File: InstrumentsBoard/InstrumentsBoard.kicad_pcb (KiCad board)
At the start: 2 copper layers, 105.7 x 47.1 mm, 27 parts, among them J1 RJ45_LED_Shielded, Q1 BSS138, Q2 BSS138, Q3 BSS138BK, U1 Teensy4.1_DEV-16771, U2 OKI

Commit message: board review changes
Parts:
- removed R8, R9: 4.7k, Resistor_SMD:R_0603_1608Metric_Pad0.98x0.95mm_HandSolder
- moved C2 12.9 mm to (107.4, 66.0), turned to -90 degrees
- moved C3 5.83 mm to (94.0, 66.2), turned to -90 degrees
- moved Conn5 2.29 mm to (65.0, 67.3)
- moved Q3 1.68 mm to (65.0, 59.8)
- moved U2 1.02 mm to (98.0, 58.0)
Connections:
- Conn5 pad 1: GND -> Net-(Q3-D)
- Conn5 pad 2: Green_Laser_5V -> +5V
- Q3 pad 1: +3V3 -> Green_Laser_3V3
- Q3 pad 2: Green_Laser_3V3 -> GND
- Q3 pad 3: Green_Laser_5V -> Net-(Q3-D)
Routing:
- net Green_Laser_5V: track 15.5 -> 0.00 mm
- net +3V3: track 152.8 -> 139.7 mm, vias 4 -> 3
- net Green_Laser_3V3: track 19.3 -> 7.37 mm
- net Net-(Q3-D): track 0.00 -> 6.96 mm
- net +5V: track 146.3 -> 147.8 mm
- net +12V: track 87.3 -> 86.2 mm
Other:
- board text removed: "5V Signal"

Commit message: fix low side toggle circuit
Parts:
- added R8: 4.7k, Resistor_SMD:R_0603_1608Metric_Pad0.98x0.95mm_HandSolder, F.Cu at (65.0, 56.4)
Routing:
- net Green_Laser_3V3: track 7.37 -> 9.83 mm
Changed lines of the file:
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@@
+  )
+  (footprint "Resistor_SMD:R_0603_1608Metric_Pad0.98x0.95mm_HandSolder" (layer "F.Cu")
+    (at 65.024 56.388 180)
+    (descr "Resistor SMD 0603 (1608 Metric), square (rectangular) end terminal, IPC_7351 nominal with elongated pad for handsoldering. (Body size source: IPC-SM-782 page 72, https://www.pcb-3d.com/wordpress/wp-content/uploads/ipc-sm-782a_amendment_1_and_2.pdf), generated with kicad-footprint-generator")
+    (tags "resistor handsolder")
+    (property "Sheetfile" "InstrumentsBoard.kicad_sch")
+    (property "Sheetname" "")
+    (property "ki_description" "Resistor")
+    (property "ki_keywords" "R res resistor")
+    (attr smd)
+    (fp_text reference "R8" (at 0 -1.43) (layer "F.SilkS")
+        (effects (font (size 1 1) (thickness 0.15)))
+    )
+    (fp_text value "4.7k" (at 0 1.43) (layer "F.Fab")
+        (effects (font (size 1 1) (thickness 0.15)))
+    )
+    (fp_text user "${REFERENCE}" (at 0 0) (layer "F.Fab")
+        (effects (font (size 0.4 0.4) (thickness 0.06)))
+    )
+    (fp_line (start -0.254724 -0.5225) (end 0.254724 -0.5225)
+      (stroke (width 0.12) (type solid)) (layer "F.SilkS"))
+    (fp_line (start -0.254724 0.5225) (end 0.254724 0.5225)
+      (stroke (width 0.12) (type solid)) (layer "F.SilkS"))
+    (fp_line (start -1.65 -0.73) (end 1.65 -0.73)
+      (stroke (width 0.05) (type solid)) (layer "F.CrtYd"))
+    (fp_line (start -1.65 0.73) (end -1.65 -0.73)
+      (stroke (width 0.05) (type solid)) (layer "F.CrtYd"))
+    (fp_line (start 1.65 -0.73) (end 1.65 0.73)
+      (stroke (width 0.05) (type solid)) (layer "F.CrtYd"))
+    (fp_line (start 1.65 0.73) (end -1.65 0.73)
+      (stroke (width 0.05) (type solid)) (layer "F.CrtYd"))
+    (fp_line (start -0.8 -0.4125) (end 0.8 -0.4125)
+      (stroke (width 0.1) (type solid)) (layer "F.Fab"))
+    (fp_line (start -0.8 0.4125) (end -0.8 -0.4125)
+      (stroke (width 0.1) (type solid)) (layer "F.Fab"))
+    (fp_line (start 0.8 -0.4125) (end 0.8 0.4125)
+      (stroke (width 0.1) (type solid)) (layer "F.Fab"))
+    (fp_line (start 0.8 0.4125) (end -0.8 0.4125)
+      (stroke (width 0.1) (type solid)) (layer "F.Fab"))
+    (pad "1" smd roundrect (at -0.9125 0 180) (size 0.975 0.95) (layers "F.Cu" "F.Paste" "F.Mask") (roundrect_rratio 0.25)
+      (net 9 "Green_Laser_3V3") (pintype "passive"))
+    (pad "2" smd roundrect (at 0.9125 0 180) (size 0.975 0.95) (layers "F.Cu" "F.Paste" "F.Mask") (roundrect_rratio 0.25)
+      (net 2 "GND") (pintype "passive"))
+    (model "${KICAD6_3DMODEL_DIR}/Resistor_SMD.3dshapes/R_0603_1608Metric.wrl"
+      (offset (xyz 0 0 0))
+      (scale (xyz 1 1 1))
+      (rotate (xyz 0 0 0))
+    )
   )
   (footprint "Resistor_SMD:R_0603_1608Metric_Pad0.98x0.95mm_HandSolder" (layer "F.Cu")
@@
   (segment (start 65.974 58.74) (end 65.974 58.831) (width 0.25) (layer "F.Cu") (net 9))
   (segment (start 71.12 53.594) (end 65.974 58.74) (width 0.25) (layer "F.Cu") (net 9))
+  (segment (start 65.9365 58.7935) (end 65.974 58.831) (width 0.25) (layer "F.Cu") (net 9))
+  (segment (start 65.9365 56.388) (end 65.9365 58.7935) (width 0.25) (layer "F.Cu") (net 9))
   (segment (start 38.899 48.223) (end 44.318 42.804) (width 0.254) (layer "F.Cu") (net 11))
   (segment (start 31.9645 47.523) (end 32.6645 48.223) (width 0.254) (layer "F.Cu") (net 11))

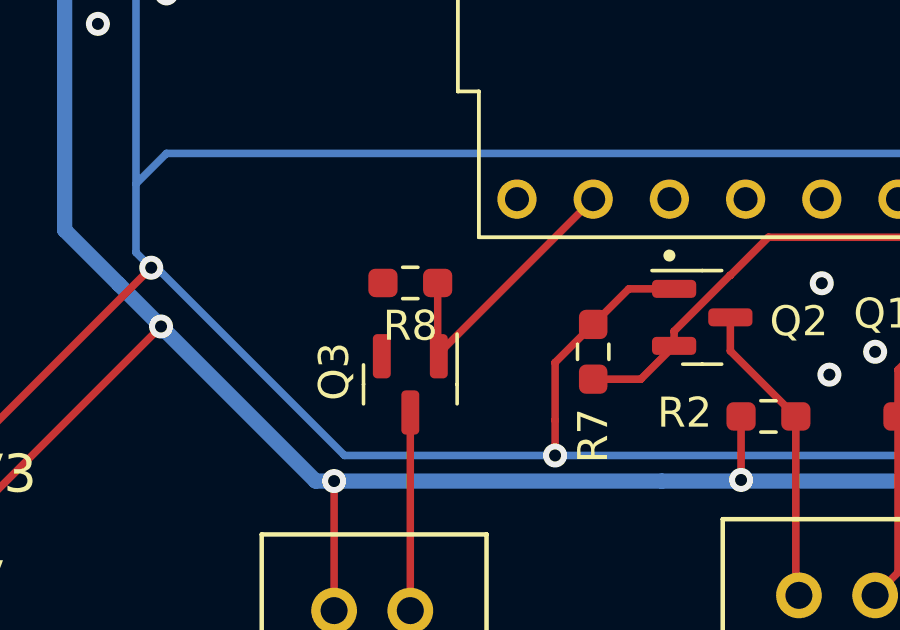
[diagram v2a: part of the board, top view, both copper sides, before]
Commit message: update laser mosfet package
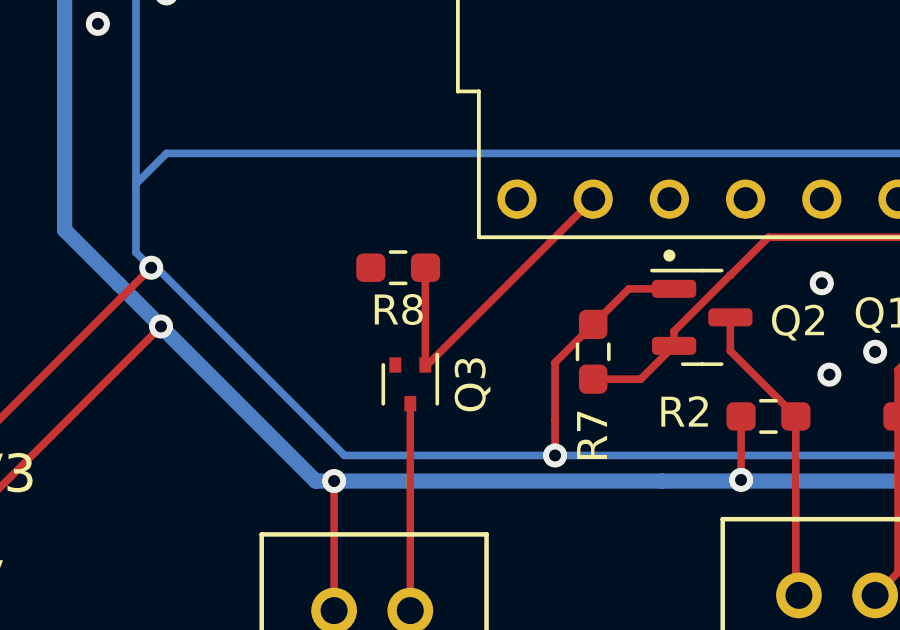
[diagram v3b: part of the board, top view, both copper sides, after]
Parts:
- Q3: footprint Package_TO_SOT_SMD:SOT-23 -> Package_TO_SOT_SMD:SOT-523
- moved R8 0.65 mm to (64.6, 55.9)
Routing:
- net Green_Laser_3V3: track 9.83 -> 10.6 mm
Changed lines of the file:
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@@
   )
   (footprint "Resistor_SMD:R_0603_1608Metric_Pad0.98x0.95mm_HandSolder" (layer "F.Cu")
-    (at 65.024 56.388 180)
+    (at 64.6195 55.88 180)
     (descr "Resistor SMD 0603 (1608 Metric), square (rectangular) end terminal, IPC_7351 nominal with elongated pad for handsoldering. (Body size source: IPC-SM-782 page 72, https://www.pcb-3d.com/wordpress/wp-content/uploads/ipc-sm-782a_amendment_1_and_2.pdf), generated with kicad-footprint-generator")
     (tags "resistor handsolder")
@@
     )
   )
-  (footprint "Package_TO_SOT_SMD:SOT-23" (layer "F.Cu")
+  (footprint "Package_TO_SOT_SMD:SOT-523" (layer "F.Cu")
     (at 65.024 59.7685 -90)
-    (descr "SOT, 3 Pin (https://www.jedec.org/system/files/docs/to-236h.pdf variant AB), generated with kicad-footprint-generator ipc_gullwing_generator.py")
-    (tags "SOT TO_SOT_SMD")
+    (descr "SOT523, https://www.diodes.com/assets/Package-Files/SOT523.pdf")
+    (tags "SOT-523")
     (property "Sheetfile" "InstrumentsBoard.kicad_sch")
     (property "Sheetname" "")
@@
     (property "ki_keywords" "N-Channel MOSFET")
     (attr smd)
-    (fp_text reference "Q3" (at -0.4295 2.54 -90) (layer "F.SilkS")
-        (effects (font (size 1 1) (thickness 0.15)))
-    )
-    (fp_text value "BSS138BK" (at 0 2.4 90) (layer "F.Fab")
-        (effects (font (size 1 1) (thickness 0.15)))
-    )
-    (fp_text user "${REFERENCE}" (at 0 0 90) (layer "F.Fab")
-        (effects (font (size 0.32 0.32) (thickness 0.05)))
-    )
-    (fp_line (start 0 -1.56) (end -1.675 -1.56)
-      (stroke (width 0.12) (type solid)) (layer "F.SilkS"))
-    (fp_line (start 0 -1.56) (end 0.65 -1.56)
-      (stroke (width 0.12) (type solid)) (layer "F.SilkS"))
-    (fp_line (start 0 1.56) (end -0.65 1.56)
-      (stroke (width 0.12) (type solid)) (layer "F.SilkS"))
-    (fp_line (start 0 1.56) (end 0.65 1.56)
-      (stroke (width 0.12) (type solid)) (layer "F.SilkS"))
-    (fp_line (start -1.92 -1.7) (end -1.92 1.7)
-      (stroke (width 0.05) (type solid)) (layer "F.CrtYd"))
-    (fp_line (start -1.92 1.7) (end 1.92 1.7)
-      (stroke (width 0.05) (type solid)) (layer "F.CrtYd"))
-    (fp_line (start 1.92 -1.7) (end -1.92 -1.7)
-      (stroke (width 0.05) (type solid)) (layer "F.CrtYd"))
-    (fp_line (start 1.92 1.7) (end 1.92 -1.7)
-      (stroke (width 0.05) (type solid)) (layer "F.CrtYd"))
-    (fp_line (start -0.65 -1.125) (end -0.325 -1.45)
-      (stroke (width 0.1) (type solid)) (layer "F.Fab"))
-    (fp_line (start -0.65 1.45) (end -0.65 -1.125)
-      (stroke (width 0.1) (type solid)) (layer "F.Fab"))
-    (fp_line (start -0.325 -1.45) (end 0.65 -1.45)
-      (stroke (width 0.1) (type solid)) (layer "F.Fab"))
-    (fp_line (start 0.65 -1.45) (end 0.65 1.45)
-      (stroke (width 0.1) (type solid)) (layer "F.Fab"))
-    (fp_line (start 0.65 1.45) (end -0.65 1.45)
-      (stroke (width 0.1) (type solid)) (layer "F.Fab"))
-    (pad "1" smd roundrect (at -0.9375 -0.95 270) (size 1.475 0.6) (layers "F.Cu" "F.Paste" "F.Mask") (roundrect_rratio 0.25)
+    (fp_text reference "Q3" (at 0 -2.032 -90) (layer "F.SilkS")
+        (effects (font (size 1 1) (thickness 0.15)))
+    )
+    (fp_text value "BSS138BK" (at 0 1.75 -90) (layer "F.Fab")
+        (effects (font (size 1 1) (thickness 0.15)))
+    )
+    (fp_text user "${REFERENCE}" (at 0 0 180) (layer "F.Fab")
+        (effects (font (size 0.4 0.4) (thickness 0.0625)))
+    )
+    (fp_line (start -1 -0.9) (end 0.65 -0.9)
+      (stroke (width 0.12) (type solid)) (layer "F.SilkS"))
+    (fp_line (start 0.65 0.9) (end -0.65 0.9)
+      (stroke (width 0.12) (type solid)) (layer "F.SilkS"))
+    (fp_line (start -1.15 -1.05) (end -1.15 1.05)
+      (stroke (width 0.05) (type solid)) (layer "F.CrtYd"))
+    (fp_line (start -1.15 -1.05) (end 1.15 -1.05)
+      (stroke (width 0.05) (type solid)) (layer "F.CrtYd"))
+    (fp_line (start 1.15 1.05) (end -1.15 1.05)
+      (stroke (width 0.05) (type solid)) (layer "F.CrtYd"))
+    (fp_line (start 1.15 1.05) (end 1.15 -1.05)
+      (stroke (width 0.05) (type solid)) (layer "F.CrtYd"))
+    (fp_line (start -0.4 -0.45) (end -0.4 0.8)
+      (stroke (width 0.1) (type solid)) (layer "F.Fab"))
+    (fp_line (start -0.4 -0.45) (end -0.05 -0.8)
+      (stroke (width 0.1) (type solid)) (layer "F.Fab"))
+    (fp_line (start -0.4 0.8) (end 0.4 0.8)
+      (stroke (width 0.1) (type solid)) (layer "F.Fab"))
+    (fp_line (start 0.4 -0.8) (end -0.05 -0.8)
+      (stroke (width 0.1) (type solid)) (layer "F.Fab"))
+    (fp_line (start 0.4 0.8) (end 0.4 -0.8)
+      (stroke (width 0.1) (type solid)) (layer "F.Fab"))
+    (pad "1" smd rect (at -0.645 -0.5 90) (size 0.51 0.4) (layers "F.Cu" "F.Paste" "F.Mask")
       (net 9 "Green_Laser_3V3") (pinfunction "G") (pintype "input"))
-    (pad "2" smd roundrect (at -0.9375 0.95 270) (size 1.475 0.6) (layers "F.Cu" "F.Paste" "F.Mask") (roundrect_rratio 0.25)
+    (pad "2" smd rect (at -0.645 0.5 90) (size 0.51 0.4) (layers "F.Cu" "F.Paste" "F.Mask")
       (net 2 "GND") (pinfunction "S") (pintype "passive"))
-    (pad "3" smd roundrect (at 0.9375 0 270) (size 1.475 0.6) (layers "F.Cu" "F.Paste" "F.Mask") (roundrect_rratio 0.25)
+    (pad "3" smd rect (at 0.645 0 90) (size 0.51 0.4) (layers "F.Cu" "F.Paste" "F.Mask")
       (net 61 "Net-(Q3-D)") (pinfunction "D") (pintype "passive"))
-    (model "${KICAD6_3DMODEL_DIR}/Package_TO_SOT_SMD.3dshapes/SOT-23.wrl"
+    (model "${KICAD6_3DMODEL_DIR}/Package_TO_SOT_SMD.3dshapes/SOT-523.wrl"
       (offset (xyz 0 0 0))
       (scale (xyz 1 1 1))
@@
   (segment (start 90.424 60.96) (end 94.432 56.952) (width 0.25) (layer "B.Cu") (net 7))
   (segment (start 94.432 56.952) (end 108.402 56.952) (width 0.25) (layer "B.Cu") (net 7))
-  (segment (start 65.974 58.74) (end 65.974 58.831) (width 0.25) (layer "F.Cu") (net 9))
-  (segment (start 71.12 53.594) (end 65.974 58.74) (width 0.25) (layer "F.Cu") (net 9))
-  (segment (start 65.9365 58.7935) (end 65.974 58.831) (width 0.25) (layer "F.Cu") (net 9))
-  (segment (start 65.9365 56.388) (end 65.9365 58.7935) (width 0.25) (layer "F.Cu") (net 9))
+  (segment (start 71.12 53.594) (end 65.5905 59.1235) (width 0.25) (layer "F.Cu") (net 9))
+  (segment (start 65.5905 59.1235) (end 65.524 59.1235) (width 0.25) (layer "F.Cu") (net 9))
+  (segment (start 65.524 56.396) (end 65.532 56.388) (width 0.25) (layer "F.Cu") (net 9))
+  (segment (start 65.524 59.1235) (end 65.524 56.396) (width 0.25) (layer "F.Cu") (net 9))
   (segment (start 38.899 48.223) (end 44.318 42.804) (width 0.254) (layer "F.Cu") (net 11))
   (segment (start 31.9645 47.523) (end 32.6645 48.223) (width 0.254) (layer "F.Cu") (net 11))
